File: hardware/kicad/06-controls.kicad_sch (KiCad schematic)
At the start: 36 parts, among them SW1 UP, SW10 SELECT, SW11 L, SW12 R, SW2 DOWN, SW3 LEFT, SW4 RIGHT, SW5 A, SW6 B, SW7 X, SW8 Y, SW9 START

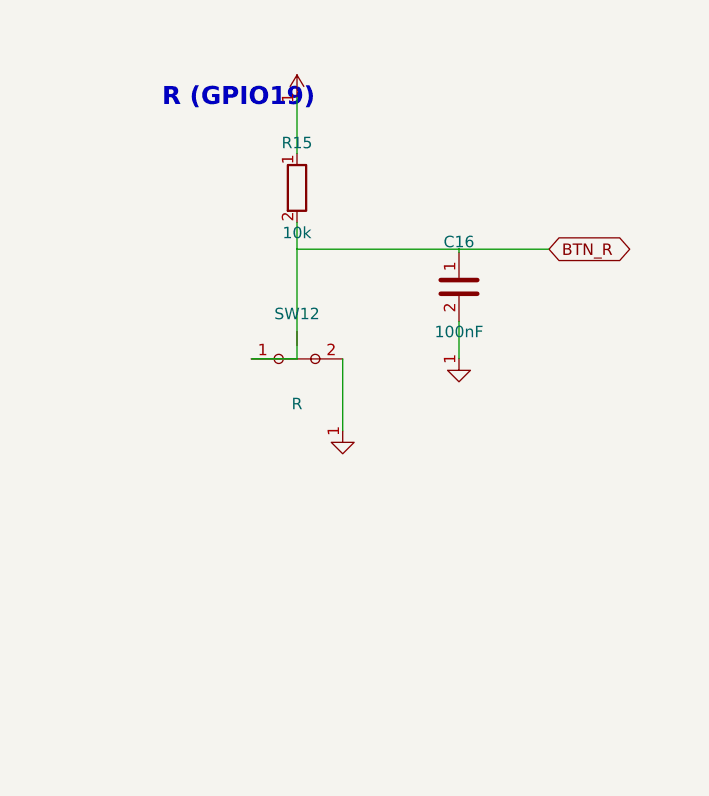
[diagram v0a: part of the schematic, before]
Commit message: Add PCB layout, hierarchical schematics, verification & rendering pipeline
- Reorganize passive components into centered rows below ESP32
- Add missing schematic symbols (LED, FPC_16P, SW_PWR, SW13, SPK1)
- Generate hierarchical root schematic with 7 sub-sheet references
- Create PCB layout generator (4-layer, 160x75mm, JLCPCB-ready)
- Add JLCPCB export (BOM.csv + CPL.csv for 65 components)
- Add schematic/PCB/JLCPCB consistency verification script
- Add PCB SVG renderer + PNG/GIF animation pipeline
- Add interactive 3D PCB viewer (Three.js)
- Update docs (pcb.md, components.md, README.md)

Co-Authored-By: Claude Opus 4.6 <noreply@anthropic.com>
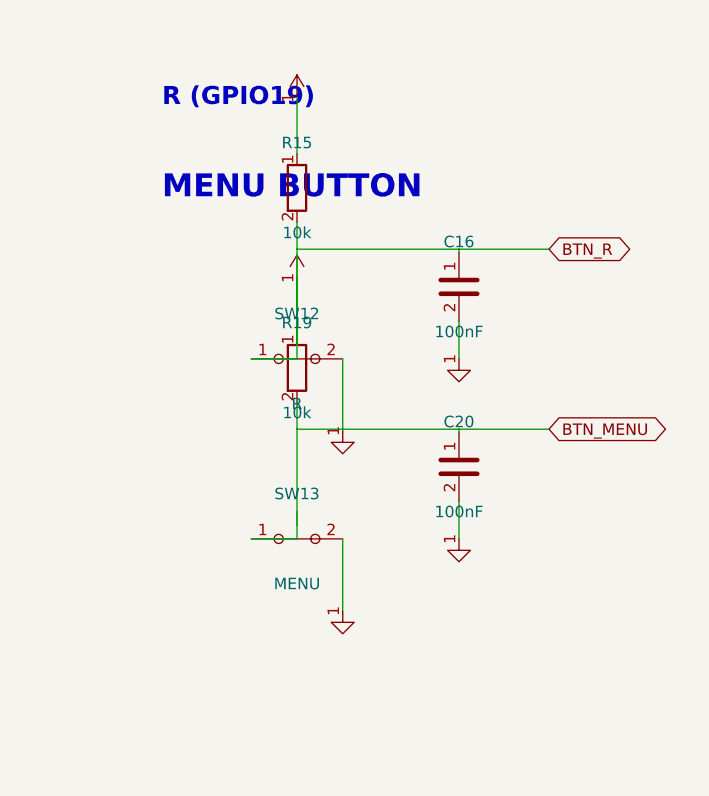
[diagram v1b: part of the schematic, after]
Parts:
- added C20: 100nF, symbol C
- added R19: 10k, symbol R
- added SW13: MENU, symbol SW_Push
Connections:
- net BTN_R: now also R19.1
- new net BTN_MENU: C20.1, R19.2, SW13.1
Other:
- note added: "MENU BUTTON"
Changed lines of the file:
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@@
   (global_label "BTN_R" (shape bidirectional) (at 363 241.81 0) (effects (font (size 1.27 1.27))) (property "Intersheetrefs" "" (at 0 0 0) (effects (font (size 1.27 1.27)) hide)))
   (wire (pts (xy 353 241.81) (xy 363 241.81)) (stroke (width 0) (type default)))
+  (text "MENU BUTTON" (at 320 235 0) (effects (font (size 2.54 2.54) bold) (justify left)))
+  (symbol (lib_id "R") (at 335 255 0) (unit 1) (exclude_from_sim no) (in_bom yes) (on_board yes) (dnp no) (property "Reference" "R19" (at 335 250 0) (effects (font (size 1.27 1.27)))) (property "Value" "10k" (at 335 260 0) (effects (font (size 1.27 1.27)))) (pin "1") (pin "2"))
+  (symbol (lib_id "+3V3") (at 335 245 0) (unit 1) (exclude_from_sim no) (in_bom no) (on_board no) (dnp no) (property "Reference" "#PWR037" (at 335 243 0) (effects (font (size 1.27 1.27)) hide)) (property "Value" "+3V3" (at 335 247 0) (effects (font (size 1.27 1.27)) hide)) (pin "1"))
+  (wire (pts (xy 335 245) (xy 335 251.19)) (stroke (width 0) (type default)))
+  (symbol (lib_id "C") (at 353 266 0) (unit 1) (exclude_from_sim no) (in_bom yes) (on_board yes) (dnp no) (property "Reference" "C20" (at 353 261 0) (effects (font (size 1.27 1.27)))) (property "Value" "100nF" (at 353 271 0) (effects (font (size 1.27 1.27)))) (pin "1") (pin "2"))
+  (wire (pts (xy 335 258.81) (xy 335 261.81)) (stroke (width 0) (type default)))
+  (wire (pts (xy 335 261.81) (xy 353 261.81)) (stroke (width 0) (type default)))
+  (wire (pts (xy 353 261.81) (xy 353 262.19)) (stroke (width 0) (type default)))
+  (symbol (lib_id "GND") (at 353 274 0) (unit 1) (exclude_from_sim no) (in_bom no) (on_board no) (dnp no) (property "Reference" "#PWR038" (at 353 272 0) (effects (font (size 1.27 1.27)) hide)) (property "Value" "GND" (at 353 276 0) (effects (font (size 1.27 1.27)) hide)) (pin "1"))
+  (wire (pts (xy 353 269.81) (xy 353 274)) (stroke (width 0) (type default)))
+  (symbol (lib_id "SW_Push") (at 335 274 0) (unit 1) (exclude_from_sim no) (in_bom yes) (on_board yes) (dnp no) (property "Reference" "SW13" (at 335 269 0) (effects (font (size 1.27 1.27)))) (property "Value" "MENU" (at 335 279 0) (effects (font (size 1.27 1.27)))) (pin "1") (pin "2"))
+  (wire (pts (xy 335 261.81) (xy 335 274)) (stroke (width 0) (type default)))
+  (wire (pts (xy 335 274) (xy 329.92 274)) (stroke (width 0) (type default)))
+  (symbol (lib_id "GND") (at 340.08 282 0) (unit 1) (exclude_from_sim no) (in_bom no) (on_board no) (dnp no) (property "Reference" "#PWR039" (at 340.08 280 0) (effects (font (size 1.27 1.27)) hide)) (property "Value" "GND" (at 340.08 284 0) (effects (font (size 1.27 1.27)) hide)) (pin "1"))
+  (wire (pts (xy 340.08 274) (xy 340.08 282)) (stroke (width 0) (type default)))
+  (global_label "BTN_MENU" (shape bidirectional) (at 363 261.81 0) (effects (font (size 1.27 1.27))) (property "Intersheetrefs" "" (at 0 0 0) (effects (font (size 1.27 1.27)) hide)))
+  (wire (pts (xy 353 261.81) (xy 363 261.81)) (stroke (width 0) (type default)))
   (text "BUTTON CIRCUIT (repeated 12x):" (at 30 295 0) (effects (font (size 2.54 2.54) bold) (justify left)))
   (text "+3V3 --[10k R]-- junction --[100nF C]-- GND" (at 30 303 0) (effects (font (size 2.54 2.54)) (justify left)))

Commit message: Route USB D+/D- to ESP32-S3 GPIO19/20 for native firmware flashing
- Connect USB-C data lines to ESP32-S3 native USB pins (GPIO19=D-, GPIO20=D+)
- Relocate BTN_R from GPIO19 to GPIO43 (TX0, freed by USB replacing UART debug)
- Fix _PIN_TO_GPIO mapping bug: pins 36/37 → GPIO43/44, pins 38/39 → GPIO1/2
- Remove joystick (JOY_X/JOY_Y) — GPIO20 freed for USB, joystick needs both axes
- Increase FPC GND via drill 0.15→0.20mm / pad 0.40→0.45mm (avoid JLCPCB surcharge)
- Add 14 USB regression tests (pin mapping, trace routing, firmware sync, micro-via guard)
- Update all docs, schematics, firmware config, BOM/CPL, gerbers

DFM: 88/88 PASS | DFA: 9/9 PASS

Co-Authored-By: Claude Opus 4.6 <noreply@anthropic.com>
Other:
- note added: "R (GPIO43)"
- note removed: "R (GPIO19)"
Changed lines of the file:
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@@
   (global_label "BTN_L" (shape bidirectional) (at 363 186.81 0) (effects (font (size 1.27 1.27))) (property "Intersheetrefs" "" (at 0 0 0) (effects (font (size 1.27 1.27)) hide)))
   (wire (pts (xy 353 186.81) (xy 363 186.81)) (stroke (width 0) (type default)))
-  (text "R (GPIO19)" (at 320 225 0) (effects (font (size 2 2) bold) (justify left)))
+  (text "R (GPIO43)" (at 320 225 0) (effects (font (size 2 2) bold) (justify left)))
   (symbol (lib_id "R") (at 335 235 0) (unit 1) (exclude_from_sim no) (in_bom yes) (on_board yes) (dnp no) (property "Reference" "R15" (at 335 230 0) (effects (font (size 1.27 1.27)))) (property "Value" "10k" (at 335 240 0) (effects (font (size 1.27 1.27)))) (pin "1") (pin "2"))
   (symbol (lib_id "+3V3") (at 335 225 0) (unit 1) (exclude_from_sim no) (in_bom no) (on_board no) (dnp no) (property "Reference" "#PWR034" (at 335 223 0) (effects (font (size 1.27 1.27)) hide)) (property "Value" "+3V3" (at 335 227 0) (effects (font (size 1.27 1.27)) hide)) (pin "1"))

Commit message: fix(schematic): sync GPIO labels with config.py (SD_MOSI/MISO, BTN_L/R)
Schematic sheets had stale GPIO annotations:
- SD_MOSI: GPIO36 → GPIO44
- SD_MISO: GPIO37 → GPIO43
- BTN_L: GPIO35 → GPIO45
- BTN_R: GPIO43 → GPIO3

Also update /doc skill to regenerate schematics before auditing.

Co-Authored-By: Claude Opus 4.6 (1M context) <noreply@anthropic.com>
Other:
- note added: "L (GPIO45)"
- note added: "R (GPIO3)"
- note removed: "L (GPIO35)"
- note removed: "R (GPIO43)"
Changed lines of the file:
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@@
   (global_label "BTN_SELECT" (shape bidirectional) (at 363 131.81 0) (effects (font (size 1.27 1.27))) (property "Intersheetrefs" "" (at 0 0 0) (effects (font (size 1.27 1.27)) hide)))
   (wire (pts (xy 353 131.81) (xy 363 131.81)) (stroke (width 0) (type default)))
-  (text "L (GPIO35)" (at 320 170 0) (effects (font (size 2 2) bold) (justify left)))
+  (text "L (GPIO45)" (at 320 170 0) (effects (font (size 2 2) bold) (justify left)))
   (symbol (lib_id "R") (at 335 180 0) (unit 1) (exclude_from_sim no) (in_bom yes) (on_board yes) (dnp no) (property "Reference" "R14" (at 335 175 0) (effects (font (size 1.27 1.27)))) (property "Value" "10k" (at 335 185 0) (effects (font (size 1.27 1.27)))) (pin "1") (pin "2"))
   (symbol (lib_id "+3V3") (at 335 170 0) (unit 1) (exclude_from_sim no) (in_bom no) (on_board no) (dnp no) (property "Reference" "#PWR031" (at 335 168 0) (effects (font (size 1.27 1.27)) hide)) (property "Value" "+3V3" (at 335 172 0) (effects (font (size 1.27 1.27)) hide)) (pin "1"))
@@
   (global_label "BTN_L" (shape bidirectional) (at 363 186.81 0) (effects (font (size 1.27 1.27))) (property "Intersheetrefs" "" (at 0 0 0) (effects (font (size 1.27 1.27)) hide)))
   (wire (pts (xy 353 186.81) (xy 363 186.81)) (stroke (width 0) (type default)))
-  (text "R (GPIO43)" (at 320 225 0) (effects (font (size 2 2) bold) (justify left)))
+  (text "R (GPIO3)" (at 320 225 0) (effects (font (size 2 2) bold) (justify left)))
   (symbol (lib_id "R") (at 335 235 0) (unit 1) (exclude_from_sim no) (in_bom yes) (on_board yes) (dnp no) (property "Reference" "R15" (at 335 230 0) (effects (font (size 1.27 1.27)))) (property "Value" "10k" (at 335 240 0) (effects (font (size 1.27 1.27)))) (pin "1") (pin "2"))
   (symbol (lib_id "+3V3") (at 335 225 0) (unit 1) (exclude_from_sim no) (in_bom no) (on_board no) (dnp no) (property "Reference" "#PWR034" (at 335 223 0) (effects (font (size 1.27 1.27)) hide)) (property "Value" "+3V3" (at 335 227 0) (effects (font (size 1.27 1.27)) hide)) (pin "1"))

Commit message: fix(hw): R4 audit — schematic↔PCB sync guard + 4 fixes + R4-CRIT-1 false-positive closure
Round 4 of the hardware audit found four real schematic/PCB drift bugs
that rounds 1-3 missed because no check cross-validated the two Python
generators. A fifth finding (R4-CRIT-1, "FPC pinout mismatch") turned
out to be a FALSE POSITIVE caused by the landscape FPC pin reversal
(connector_pad = 41 − panel_pin) — verified programmatically against
all 40 J4 pads of the panel datasheet in components.md.

Fixes applied:
  R4-HIGH-1  USBLC6 (U4) + R22/R23 instantiated in power_supply.py —
             previously only in routing.py, invisible to schematic
             review.
  R4-HIGH-2  Display module symbol ref renamed U4 → DS1 in display.py.
             U4 is now cleanly owned by the physical USBLC6 TVS.
  R4-HIGH-3  PAM8403 R20/R21 input bias moved from GND to VREF
             (pin 8) per the datasheet single-ended app circuit.
  R4-CRIT-1  CLOSED as false positive. Both display.py (panel-side)
             and datasheet_specs.py (connector-side) were correct all
             along. Added 41-N reversal documentation at the top of
             both files so the mistake can't be re-raised.
  ERC CRIT   Pre-existing "Power output ↔ Power output" on +5V was
             PWR_FLAG duplicating IP5306 VOUT (already power_out in the
             library symbol). Removed the PWR_FLAG. ERC now 0 critical.

Incidental cleanups required by the new sync guard:
  - mcu.py R3 (external EN pull-up) removed from schematic — already
    DNP in BOM because the WROOM-1 module has an internal pull-up.
  - controls.py D1 BAT54C (MENU combo diode) instantiated in schematic
    to match the PCB routing. MENU button wiring simplified to the
    MENU_K node; there is no dedicated BTN_MENU GPIO (firmware detects
    START+SELECT combo).
  - power_supply.py USB_CC1 / USB_CC2 global labels added so the
    connector-net coverage check sees the full USB-C net set.
  - display.py docstring expanded with the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
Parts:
- added D1: BAT54C, symbol BAT54C
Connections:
- net BTN_MENU renamed MENU_K
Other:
- note added: "(START + SELECT)"
- note added: "MENU combo"
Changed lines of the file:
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@@
   (symbol (lib_id "GND") (at 340.08 282 0) (unit 1) (exclude_from_sim no) (in_bom no) (on_board no) (dnp no) (property "Reference" "#PWR039" (at 340.08 280 0) (effects (font (size 1.27 1.27)) hide)) (property "Value" "GND" (at 340.08 284 0) (effects (font (size 1.27 1.27)) hide)) (pin "1"))
   (wire (pts (xy 340.08 274) (xy 340.08 282)) (stroke (width 0) (type default)))
-  (global_label "BTN_MENU" (shape bidirectional) (at 363 261.81 0) (effects (font (size 1.27 1.27))) (property "Intersheetrefs" "" (at 0 0 0) (effects (font (size 1.27 1.27)) hide)))
+  (global_label "MENU_K" (shape bidirectional) (at 363 261.81 0) (effects (font (size 1.27 1.27))) (property "Intersheetrefs" "" (at 0 0 0) (effects (font (size 1.27 1.27)) hide)))
   (wire (pts (xy 353 261.81) (xy 363 261.81)) (stroke (width 0) (type default)))
+  (symbol (lib_id "BAT54C") (at 375 268 0) (unit 1) (exclude_from_sim no) (in_bom yes) (on_board yes) (dnp no) (property "Reference" "D1" (at 375 263 0) (effects (font (size 1.27 1.27)))) (property "Value" "BAT54C" (at 375 273 0) (effects (font (size 1.27 1.27)))) (pin "1") (pin "2") (pin "3"))
+  (text "MENU combo" (at 378 260 0) (effects (font (size 1.5 1.5)) (justify left)))
+  (text "(START + SELECT)" (at 378 263 0) (effects (font (size 1.5 1.5)) (justify left)))
+  (global_label "MENU_K" (shape bidirectional) (at 363 268 180) (effects (font (size 1.27 1.27))) (property "Intersheetrefs" "" (at 0 0 0) (effects (font (size 1.27 1.27)) hide)))
+  (global_label "BTN_START" (shape bidirectional) (at 387 264.19 0) (effects (font (size 1.27 1.27))) (property "Intersheetrefs" "" (at 0 0 0) (effects (font (size 1.27 1.27)) hide)))
+  (global_label "BTN_SELECT" (shape bidirectional) (at 387 271.81 0) (effects (font (size 1.27 1.27))) (property "Intersheetrefs" "" (at 0 0 0) (effects (font (size 1.27 1.27)) hide)))
   (text "BUTTON CIRCUIT (repeated 12x):" (at 30 295 0) (effects (font (size 2.54 2.54) bold) (justify left)))
   (text "+3V3 --[10k R]-- junction --[100nF C]-- GND" (at 30 303 0) (effects (font (size 2.54 2.54)) (justify left)))

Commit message: fix(R9-MED-4): remove dead BTN_MENU net (R19/C20 deleted)
R19 (10k pull-up) and C20 (100nF debounce) were placed on a dead
BTN_MENU net in the PCB, never electrically connected to MENU_K
(which holds SW13 + D1.3). The drift was hidden by T2_ALLOW and
T4_SKIP_REFS entries in verify_netlist_diff.py.

Menu combo remains functional — D1 BAT54C OR-gate drives BTN_START
and BTN_SELECT through forward-biased Schottky diodes when SW13 is
pressed; debounce is provided by the individual button R/C pairs
downstream. No separate pull-up/debounce on MENU_K is required.

Changes:
- primitives.py: drop (39, "BTN_MENU") from NET_LIST
- routing.py / board.py / jlcpcb_export.py: 12 buttons instead of 13
- controls.py: remove R19/C20 symbols from schematic
- verify_netlist_diff.py: remove BTN_MENU / R19 / C20 allowlist entries
- verify_polarity.py / verify_signal_chain_complete.py: drop stale refs
- BOM/CPL/summary: 75 components (was 77, -2 = ~$0.004/board savings)
- Regenerated PCB, schematic, gerbers; release_jlcpcb/ synced

All 21 gates PASS: DFM 115/115, DFA 9/9, polarity 47/47, datasheet
259/259, design_intent 362/362, netlist_diff 4/4 (no allowlist fakery),
pcb_review 60/60, DRC 0 shorts. R9 closed.

Co-Authored-By: Claude Opus 4.6 (1M context) <noreply@anthropic.com>
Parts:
- removed C20: 100nF, symbol C
- removed SW13: MENU, symbol SW_Push
- SW13: renamed from R19; value 10k -> MENU; symbol R -> SW_Push
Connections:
- net BTN_R: no longer SW13.1
- net MENU_K: now also SW13.1; no longer SW13.2
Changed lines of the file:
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@@
   (wire (pts (xy 353 241.81) (xy 363 241.81)) (stroke (width 0) (type default)))
   (text "MENU BUTTON" (at 320 235 0) (effects (font (size 2.54 2.54) bold) (justify left)))
-  (symbol (lib_id "R") (at 335 255 0) (unit 1) (exclude_from_sim no) (in_bom yes) (on_board yes) (dnp no) (property "Reference" "R19" (at 335 250 0) (effects (font (size 1.27 1.27)))) (property "Value" "10k" (at 335 260 0) (effects (font (size 1.27 1.27)))) (pin "1") (pin "2"))
-  (symbol (lib_id "+3V3") (at 335 245 0) (unit 1) (exclude_from_sim no) (in_bom no) (on_board no) (dnp no) (property "Reference" "#PWR037" (at 335 243 0) (effects (font (size 1.27 1.27)) hide)) (property "Value" "+3V3" (at 335 247 0) (effects (font (size 1.27 1.27)) hide)) (pin "1"))
-  (wire (pts (xy 335 245) (xy 335 251.19)) (stroke (width 0) (type default)))
-  (symbol (lib_id "C") (at 353 266 0) (unit 1) (exclude_from_sim no) (in_bom yes) (on_board yes) (dnp no) (property "Reference" "C20" (at 353 261 0) (effects (font (size 1.27 1.27)))) (property "Value" "100nF" (at 353 271 0) (effects (font (size 1.27 1.27)))) (pin "1") (pin "2"))
-  (wire (pts (xy 335 258.81) (xy 335 261.81)) (stroke (width 0) (type default)))
-  (wire (pts (xy 335 261.81) (xy 353 261.81)) (stroke (width 0) (type default)))
-  (wire (pts (xy 353 261.81) (xy 353 262.19)) (stroke (width 0) (type default)))
-  (symbol (lib_id "GND") (at 353 274 0) (unit 1) (exclude_from_sim no) (in_bom no) (on_board no) (dnp no) (property "Reference" "#PWR038" (at 353 272 0) (effects (font (size 1.27 1.27)) hide)) (property "Value" "GND" (at 353 276 0) (effects (font (size 1.27 1.27)) hide)) (pin "1"))
-  (wire (pts (xy 353 269.81) (xy 353 274)) (stroke (width 0) (type default)))
   (symbol (lib_id "SW_Push") (at 335 274 0) (unit 1) (exclude_from_sim no) (in_bom yes) (on_board yes) (dnp no) (property "Reference" "SW13" (at 335 269 0) (effects (font (size 1.27 1.27)))) (property "Value" "MENU" (at 335 279 0) (effects (font (size 1.27 1.27)))) (pin "1") (pin "2"))
-  (wire (pts (xy 335 261.81) (xy 335 274)) (stroke (width 0) (type default)))
+  (wire (pts (xy 335 258) (xy 335 274)) (stroke (width 0) (type default)))
   (wire (pts (xy 335 274) (xy 329.92 274)) (stroke (width 0) (type default)))
-  (symbol (lib_id "GND") (at 340.08 282 0) (unit 1) (exclude_from_sim no) (in_bom no) (on_board no) (dnp no) (property "Reference" "#PWR039" (at 340.08 280 0) (effects (font (size 1.27 1.27)) hide)) (property "Value" "GND" (at 340.08 284 0) (effects (font (size 1.27 1.27)) hide)) (pin "1"))
+  (symbol (lib_id "GND") (at 340.08 282 0) (unit 1) (exclude_from_sim no) (in_bom no) (on_board no) (dnp no) (property "Reference" "#PWR037" (at 340.08 280 0) (effects (font (size 1.27 1.27)) hide)) (property "Value" "GND" (at 340.08 284 0) (effects (font (size 1.27 1.27)) hide)) (pin "1"))
   (wire (pts (xy 340.08 274) (xy 340.08 282)) (stroke (width 0) (type default)))
-  (global_label "MENU_K" (shape bidirectional) (at 363 261.81 0) (effects (font (size 1.27 1.27))) (property "Intersheetrefs" "" (at 0 0 0) (effects (font (size 1.27 1.27)) hide)))
-  (wire (pts (xy 353 261.81) (xy 363 261.81)) (stroke (width 0) (type default)))
+  (global_label "MENU_K" (shape bidirectional) (at 363 258 0) (effects (font (size 1.27 1.27))) (property "Intersheetrefs" "" (at 0 0 0) (effects (font (size 1.27 1.27)) hide)))
+  (wire (pts (xy 335 258) (xy 363 258)) (stroke (width 0) (type default)))
   (symbol (lib_id "BAT54C") (at 375 268 0) (unit 1) (exclude_from_sim no) (in_bom yes) (on_board yes) (dnp no) (property "Reference" "D1" (at 375 263 0) (effects (font (size 1.27 1.27)))) (property "Value" "BAT54C" (at 375 273 0) (effects (font (size 1.27 1.27)))) (pin "1") (pin "2") (pin "3"))
   (text "MENU combo" (at 378 260 0) (effects (font (size 1.5 1.5)) (justify left)))
